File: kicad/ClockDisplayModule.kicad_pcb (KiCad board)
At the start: 2 copper layers, 88.9 x 54.6 mm, 41 parts, among them IC101 ATMEGA8-P, P101 CONN_02X03, P102 CONN_01X05, P201 CONN_01X06, P202 CONN_01X07, P203 CONN_01X06, P204 CONN_01X07, Q201 BC856BS, Q202 BC856BS, Q203 BC856BS, U201 SN74LS138, U202 74HC4511

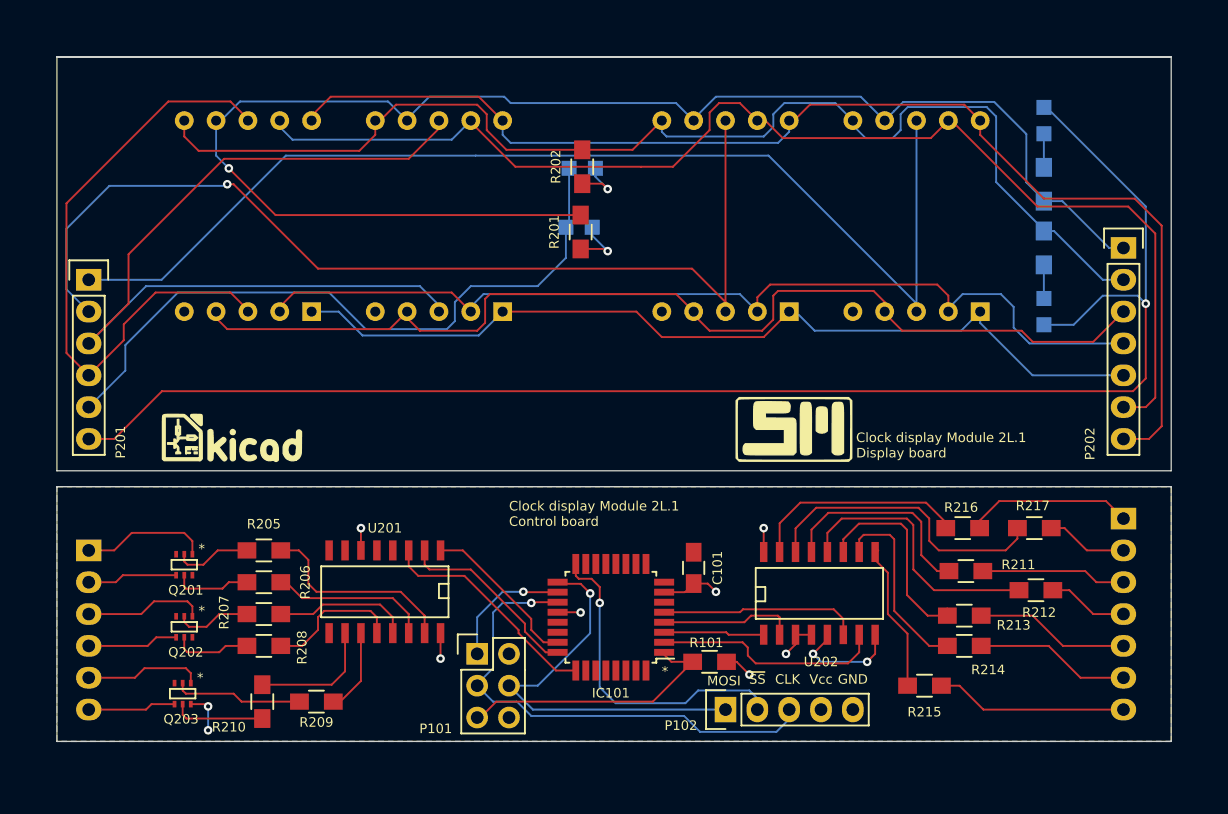
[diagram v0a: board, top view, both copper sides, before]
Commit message: Added breakout for the board
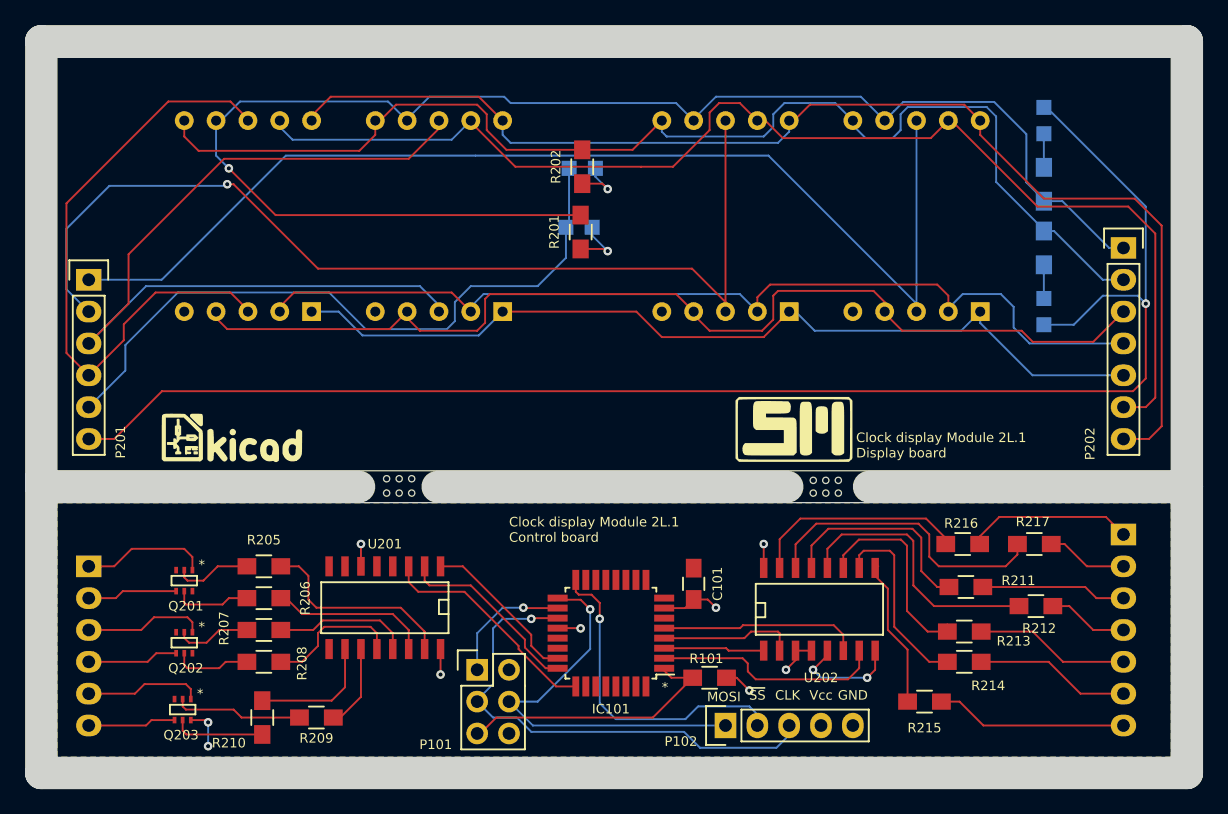
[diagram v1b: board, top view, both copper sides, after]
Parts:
- added MouseBite: VAL**, ClockFootprints:MouseBite-npth, F.Cu at (144.1, 76.8)
- added MouseBite: VAL**, ClockFootprints:MouseBite-npth, F.Cu at (144.1, 78.0)
- added MouseBite: VAL**, ClockFootprints:MouseBite-npth, F.Cu at (178.2, 77.0)
- added MouseBite: VAL**, ClockFootprints:MouseBite-npth, F.Cu at (178.2, 78.0)
- moved R207 1.27 mm to (133.3, 88.9)
- moved R209 1.27 mm to (137.5, 95.9)
- moved R210 1.27 mm to (133.2, 95.9)
- moved R211 1.27 mm to (189.4, 85.5)
- moved R212 1.27 mm to (194.9, 87.0)
- moved C101 1.27 mm to (167.6, 85.2)
- moved IC101 1.27 mm to (161.0, 89.2)
- moved P101 1.27 mm to (150.4, 92.1)
- moved P102 1.27 mm to (170.2, 96.5)
- moved P203 1.27 mm to (119.4, 83.8)
- moved P204 1.27 mm to (201.9, 81.3)
- moved Q201 1.27 mm to (127.0, 85.0)
- moved Q202 1.27 mm to (127.0, 89.9)
- moved Q203 1.27 mm to (126.9, 95.2)
- moved R101 1.27 mm to (168.9, 92.7)
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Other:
- board size 88.9 x 54.6 mm -> 91.4 x 58.4 mm

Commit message: Updated the logo
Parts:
- removed the G*** at (175.6, 72.9)
- added G***: LOGO, ClockFootprints:myLogo_7mm, F.Cu at (176.5, 73.0)

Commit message: More refinements and updates to logos
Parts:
- removed the G*** at (176.5, 73.0)
- removed MouseBite (x4): VAL**, ClockFootprints:MouseBite-npth
- added G***: LOGO, ClockFootprints:myLogo_basic_50, F.Cu at (176.7, 73.0)
- added REF**: MouseBite, ClockFootprints:MouseBite, F.Cu at (143.0, 78.4)
- added REF**: MouseBite, ClockFootprints:MouseBite, F.Cu at (177.3, 78.4)
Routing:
- net Net-(R217-Pad2): track 24.0 -> 22.5 mm
- net Net-(R211-Pad2): track 17.2 -> 16.5 mm
- net A2: track 18.2 -> 17.5 mm
- net A1: track 15.0 -> 14.5 mm
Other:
- outline, holes or cut-outs redrawn
- net class Default: clearance 0.254 -> 0.1524
- rule trace_clearance: 0.254 -> 0.1524
- board text added: "1"

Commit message: Final logo added
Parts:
- removed the G*** at (176.7, 73.0)
- added G***: LOGO, ClockFootprints:myLogo_basic_rounded_50, F.Cu at (176.9, 72.9)

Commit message: Changes to the gerbers
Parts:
- moved D201 0.25 mm to (158.8, 56.8)
- moved R201 0.13 mm to (158.8, 57.1)
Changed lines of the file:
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@@
     (pad_drill 0.6)
     (pad_to_mask_clearance 0)
+    (pad_to_paste_clearance 0.0254)
     (aux_axis_origin 0 0)
     (visible_elements FFFEFF7F)
@@
   )
   (module LEDs:LED-0805 (layer B.Cu)
-    (at 158.496 56.769)
+    (at 158.75 56.769)
     (descr "LED 0805 smd package")
     (tags "LED 0805 SMD")
@@
   )
   (module Resistors_SMD:R_0805_HandSoldering (layer F.Cu)
-    (at 158.623 57.15 90)
+    (at 158.75 57.15 90)
     (descr "Resistor SMD 0805, hand soldering")
     (tags "resistor 0805")
@@
   (segment (start 197.057 54.69) (end 200.787 58.42) (width 0.3048) (layer B.Cu) (net 6))
   (segment (start 200.787 58.42) (end 201.93 58.42) (width 0.3048) (layer B.Cu) (net 6))
-  (segment (start 158.623 55.8) (end 134.286 55.8) (width 0.3048) (layer F.Cu) (net 6))
+  (segment (start 158.75 55.8) (end 134.286 55.8) (width 0.3048) (layer F.Cu) (net 6) (status 10))
   (segment (start 134.286 55.8) (end 130.556 52.07) (width 0.3048) (layer F.Cu) (net 6))
   (via (at 130.556 52.07) (size 0.6858) (drill 0.3302) (layers F.Cu B.Cu) (net 6))
@@
   (segment (start 177.165 92.075) (end 177.8 92.71) (width 0.3048) (layer B.Cu) (net 13))
   (via (at 177.165 92.075) (size 0.6858) (drill 0.3302) (layers F.Cu B.Cu) (net 13))
-  (segment (start 159.54502 56.769) (end 159.54502 57.43702) (width 0.3048) (layer B.Cu) (net 14))
-  (segment (start 159.54502 57.43702) (end 160.782 58.674) (width 0.3048) (layer B.Cu) (net 14))
+  (segment (start 159.79902 56.769) (end 159.79902 57.69102) (width 0.3048) (layer B.Cu) (net 14))
   (via (at 160.782 58.674) (size 0.6858) (drill 0.3302) (layers F.Cu B.Cu) (net 14))
   (segment (start 160.782 58.674) (end 160.608 58.5) (width 0.3048) (layer F.Cu) (net 14))
-  (segment (start 160.608 58.5) (end 158.623 58.5) (width 0.3048) (layer F.Cu) (net 14))
+  (segment (start 160.608 58.5) (end 158.75 58.5) (width 0.3048) (layer F.Cu) (net 14) (status 20))
+  (segment (start 159.79902 57.69102) (end 160.782 58.674) (width 0.3048) (layer B.Cu) (net 14))
+  (segment (start 157.70098 56.769) (end 157.70098 52.07) (width 0.3048) (layer B.Cu) (net 15))
+  (segment (start 155.194 61.468) (end 155.194 59.27598) (width 0.3048) (layer B.Cu) (net 15))
+  (segment (start 155.194 61.468) (end 149.86 61.468) (width 0.3048) (layer B.Cu) (net 15))
+  (segment (start 149.86 61.468) (end 148.59 62.738) (width 0.3048) (layer B.Cu) (net 15))
+  (segment (start 148.59 62.738) (end 148.59 64.262) (width 0.3048) (layer B.Cu) (net 15))
+  (segment (start 148.59 64.262) (end 147.955 64.897) (width 0.3048) (layer B.Cu) (net 15))
+  (segment (start 147.955 64.897) (end 141.478 64.897) (width 0.3048) (layer B.Cu) (net 15))
+  (segment (start 141.478 64.897) (end 138.557 61.976) (width 0.3048) (layer B.Cu) (net 15))
+  (segment (start 119.38 71.12) (end 122.301 68.199) (width 0.3048) (layer B.Cu) (net 15))
+  (segment (start 122.301 66.167) (end 122.301 68.199) (width 0.3048) (layer B.Cu) (net 15))
+  (segment (start 126.492 61.976) (end 122.301 66.167) (width 0.3048) (layer B.Cu) (net 15))
   (segment (start 138.557 61.976) (end 126.492 61.976) (width 0.3048) (layer B.Cu) (net 15))
-  (segment (start 126.492 61.976) (end 122.301 66.167) (width 0.3048) (layer B.Cu) (net 15))
-  (segment (start 122.301 66.167) (end 122.301 68.199) (width 0.3048) (layer B.Cu) (net 15))
-  (segment (start 122.301 68.199) (end 119.38 71.12) (width 0.3048) (layer B.Cu) (net 15))
-  (segment (start 157.44698 56.769) (end 157.44698 59.21502) (width 0.3048) (layer B.Cu) (net 15))
-  (segment (start 141.478 64.897) (end 138.557 61.976) (width 0.3048) (layer B.Cu) (net 15))
-  (segment (start 147.955 64.897) (end 141.478 64.897) (width 0.3048) (layer B.Cu) (net 15))
-  (segment (start 148.59 64.262) (end 147.955 64.897) (width 0.3048) (layer B.Cu) (net 15))
-  (segment (start 148.59 62.738) (end 148.59 64.262) (width 0.3048) (layer B.Cu) (net 15))
-  (segment (start 149.86 61.468) (end 148.59 62.738) (width 0.3048) (layer B.Cu) (net 15))
-  (segment (start 155.194 61.468) (end 149.86 61.468) (width 0.3048) (layer B.Cu) (net 15))
-  (segment (start 157.44698 59.21502) (end 155.194 61.468) (width 0.3048) (layer B.Cu) (net 15))
-  (segment (start 157.70098 52.07) (end 157.70098 56.515) (width 0.3048) (layer B.Cu) (net 15))
-  (segment (start 157.70098 56.515) (end 157.44698 56.769) (width 0.1524) (layer B.Cu) (net 15))
+  (segment (start 155.194 59.27598) (end 157.70098 56.769) (width 0.3048) (layer B.Cu) (net 15))
+  (segment (start 157.95498 56.515) (end 157.70098 56.769) (width 0.1524) (layer B.Cu) (net 15) (status 30))
   (segment (start 159.79902 52.07) (end 159.79902 52.73802) (width 0.3048) (layer B.Cu) (net 16))
   (segment (start 159.79902 52.73802) (end 160.782 53.721) (width 0.3048) (layer B.Cu) (net 16))

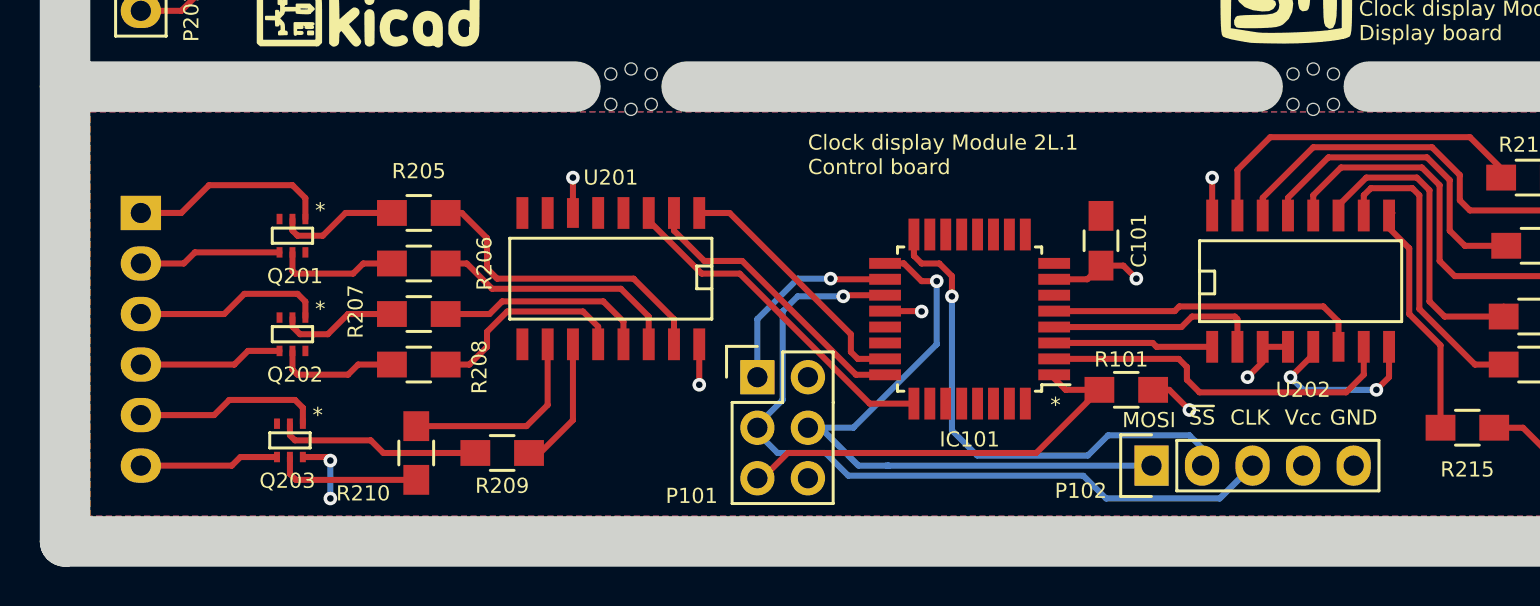
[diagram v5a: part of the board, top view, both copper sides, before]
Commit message: Correction to microcontroller footprint
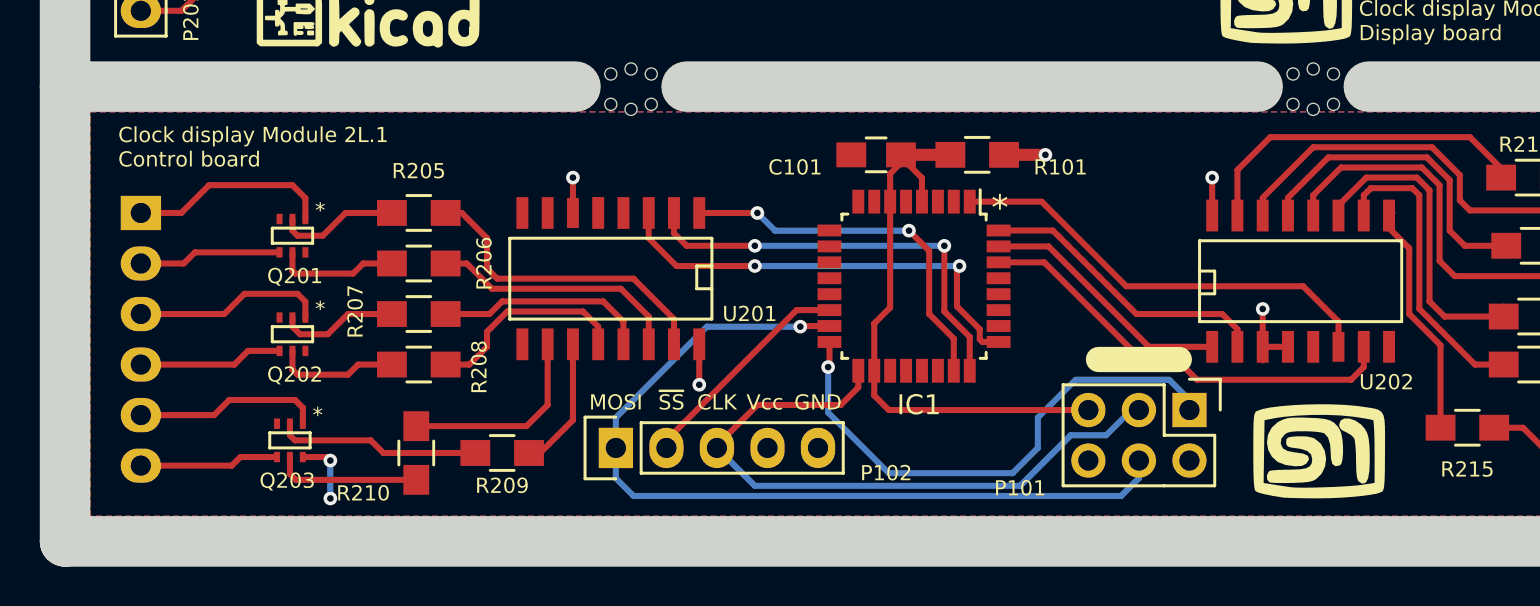
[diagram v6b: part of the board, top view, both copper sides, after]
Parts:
- removed IC101: ATMEGA8-P, Housings_QFP:TQFP-32_7x7mm_Pitch0.8mm
- added G***: LOGO, ClockFootprints:myLogo_basic_rounded_50, F.Cu at (178.6, 95.8)
- added IC1: ATMEGA88PA-A, Housings_QFP:LQFP-32_7x7mm_Pitch0.8mm, F.Cu at (158.2, 87.5)
- moved P102 26.9 mm to (143.3, 95.6)
- moved P101 21.8 mm to (172.1, 93.7), turned to 270 degrees
- moved R101 14.0 mm to (161.4, 80.9), turned to 0 degrees
- moved C101 12.1 mm to (156.3, 80.9), turned to 180 degrees
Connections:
- C101 pad 1: VCC -> Reset
- R101 pad 1: VCC -> Reset
- R101 pad 2: Reset -> VCC
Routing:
- net MISO: track 10.2 -> 26.8 mm
- net ~SS: track 25.9 -> 11.4 mm, vias 1 -> 0
- net MOSI: track 32.7 -> 44.2 mm
- net GND: track 12.4 -> 3.74 mm, vias 4 -> 2
- net A1: track 14.5 -> 22.3 mm, vias 0 -> 2
- net Reset: track 21.7 -> 29.0 mm
- net D: track 16.0 -> 22.3 mm
- net CLK: track 39.1 -> 32.9 mm, vias 1 -> 0
- net A0: track 12.9 -> 18.9 mm, vias 0 -> 2
- net VCC: track 17.6 -> 11.7 mm, vias 7 -> 5
- net A2: track 17.5 -> 23.1 mm, vias 0 -> 2
- net B: track 8.02 -> 12.8 mm
- net C: track 10.9 -> 14.9 mm
- net A: track 18.4 -> 22.1 mm
